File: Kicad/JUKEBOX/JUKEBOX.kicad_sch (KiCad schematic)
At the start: 34 parts, among them J1 Entrada 5V, J10 Fader volumen (B10K), J2 Salida 5V a P4 CIAA, J3 OLED SH1106 I2C, J4 RFID RC522, J5 Parlante respaldo (mono), J6 Alim. PAM8403, J7 Audio a PAM8403, J8 ULN2003 IN1-IN4, J9 ULN2003 alimentación, U1 DFPlayer_Mini, U2 24LC256

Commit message: Actualizacion: neopixel + buffer 74AHCT125
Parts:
- added C14: 100 nF, symbol Device:C
- added C15: 470 µF / 16 V, symbol Device:C_Polarized
- added J11: NeoPixel, symbol Connector_Generic:Conn_01x03
- added R9: 330 Ω, symbol Device:R
- added U4: 74AHCT125, Package_CSP:Xilinx_CSG48_7.0x7.0mm_Layout7x7_P0.8mm, symbol 74xx:74AHCT125
- renumbered R4 to R3, R5 to R4, R6 to R5, R7 to R6, R8 to R7, R9 to R8
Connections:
- net +5V: now also C14.1, C15.1, J11.1 (Pin_1), U4.10, U4.13, U4.14 (VCC), U4.4
- net GND: now also C14.2, C15.2, J11.3 (Pin_3), U4.1, U4.12, U4.5, U4.7 (GND), U4.9
- net NEO_DATA: now reaches XA1.36 (tecF1)
- net NEO_DATA: now also U4.2
- new net: R9.1, U4.3
- new net NEO_DIN: J11.2 (Pin_2), R9.2
- no-connect marks 47 -> 49
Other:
- moved on the sheet: C10, C11, C12, C13, C3, C4, C5, C6, C7, C8, C9, J10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

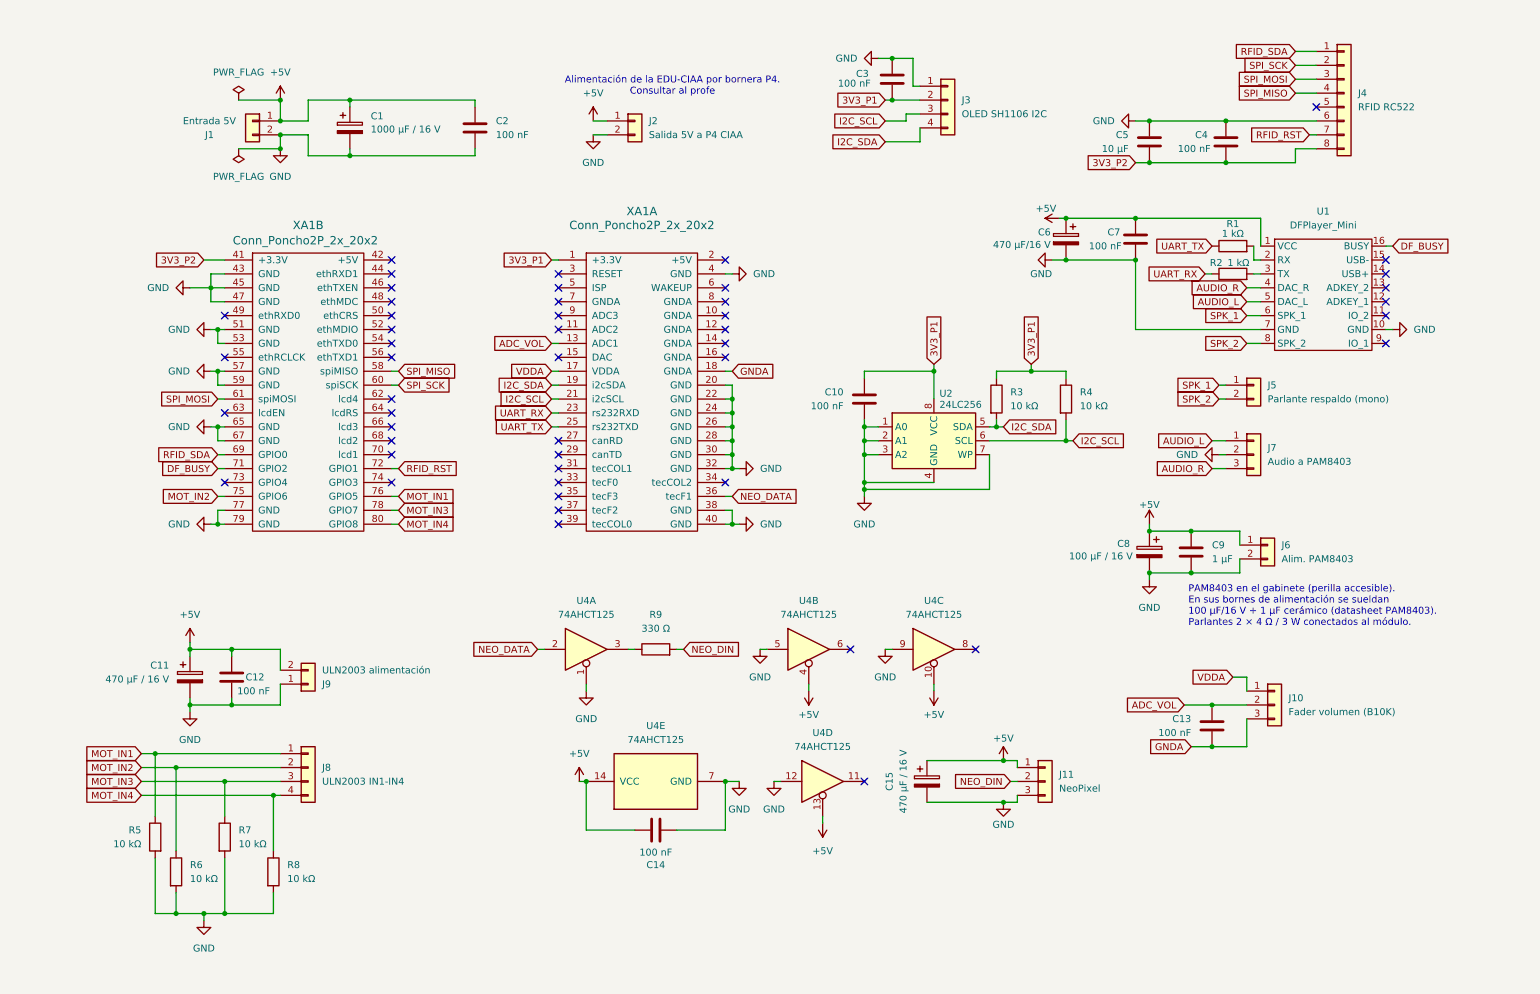
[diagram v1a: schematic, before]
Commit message: Actualizacion de esquematico sobre correciones de Jose y redaccion de informe de avance.
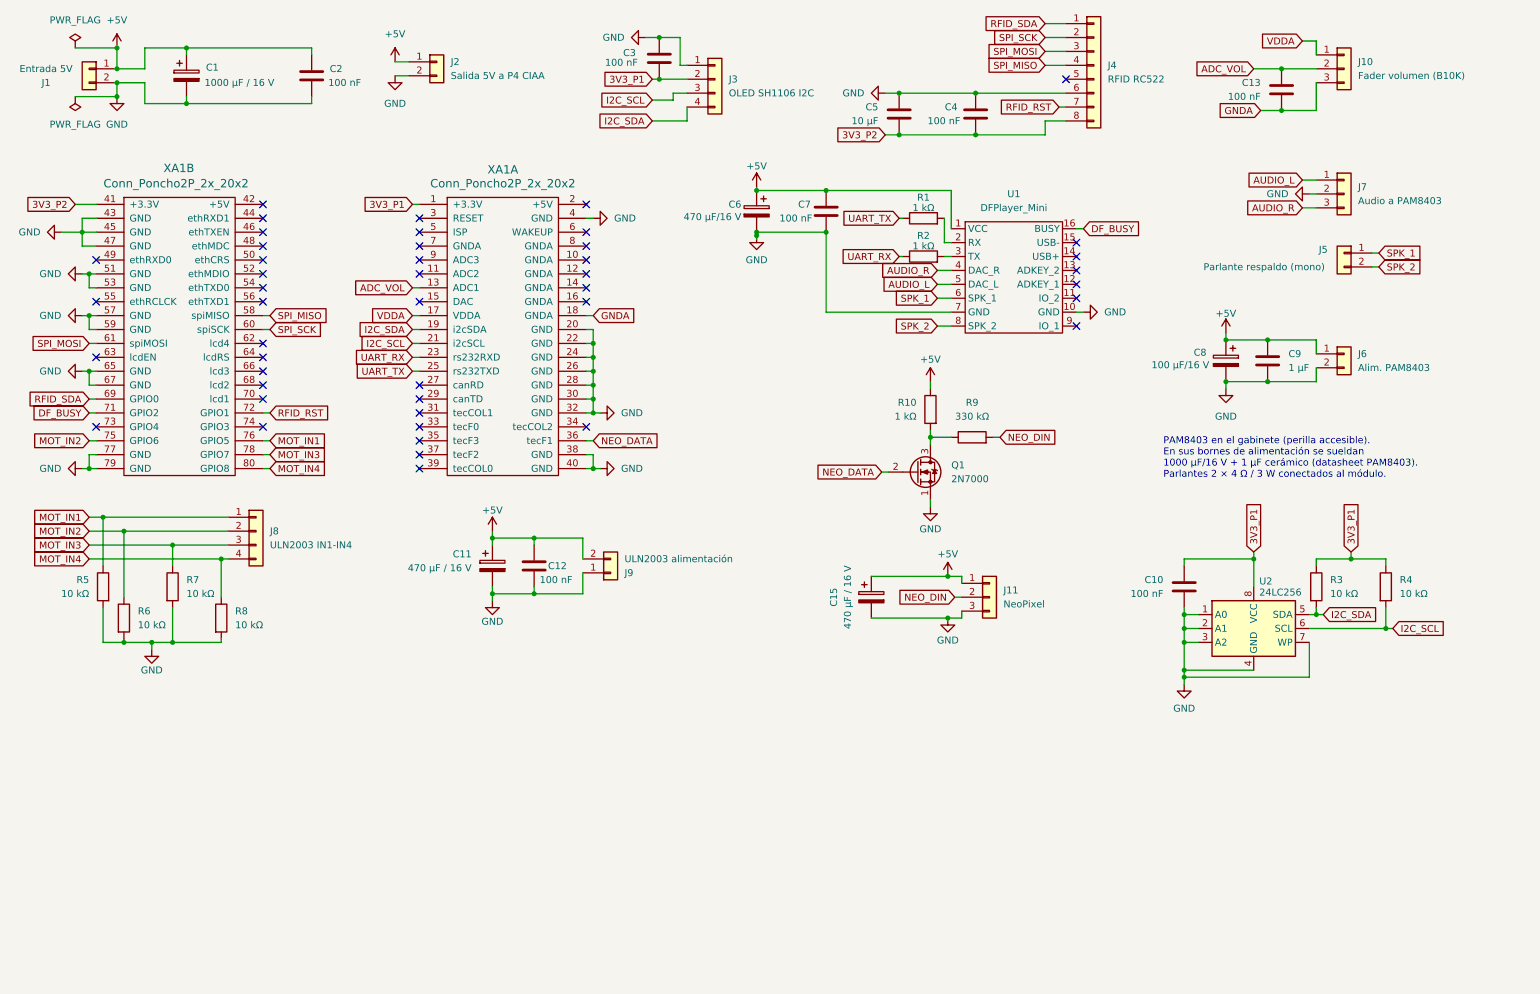
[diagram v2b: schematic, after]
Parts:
- removed C14: 100 nF, symbol Device:C
- removed U4: 74AHCT125, Package_CSP:Xilinx_CSG48_7.0x7.0mm_Layout7x7_P0.8mm, symbol 74xx:74AHCT125
- added Q1: 2N7000, Package_TO_SOT_THT:TO-92_Inline, symbol Transistor_FET:2N7000
- added R10: 1 kΩ, Package_TO_SOT_THT:TO-92_Inline, symbol Device:R
- C8: value 100 µF / 16 V -> 100 µF/16 V
- R9: value 330 Ω -> 330 kΩ; footprint (none) -> Package_TO_SOT_THT:TO-92_Inline
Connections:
- net +5V: now also R10.1
- net GND: now also Q1.1 (S)
- net NEO_DATA: now also Q1.2 (G)
- net at R9.1: now also Q1.3 (D), R10.2
- no-connect marks 49 -> 46
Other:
- note added: "PAM8403 en el gabinete (perilla accesible). En sus bornes de alimentación se sueldan 1000 µF/16 V + 1 µF cerámico (datasheet PAM8403). Parlantes 2 × 4 Ω / 3 W conectados al módulo."
- note removed: "Alimentación de la EDU-CIAA por bornera P4. Consultar al profe"
- note removed: "PAM8403 en el gabinete (perilla accesible). En sus bornes de alimentación se sueldan 100 µF/16 V + 1 µF cerámico (datasheet PAM8403). Parlantes 2 × 4 Ω / 3 W conectados al módulo."
- company: (none) -> Acuña, Avila Montoya, Bejarano, Seijo
- title: (none) -> Tocadisco digital
- moved on the sheet: C1, C10, C11, C12, C13, C15, C2, C3, C4, C5, C6, C7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
